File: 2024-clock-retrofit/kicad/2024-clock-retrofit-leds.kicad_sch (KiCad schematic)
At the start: 60 parts, among them Q1 AO3400A, Q2 AO3400A

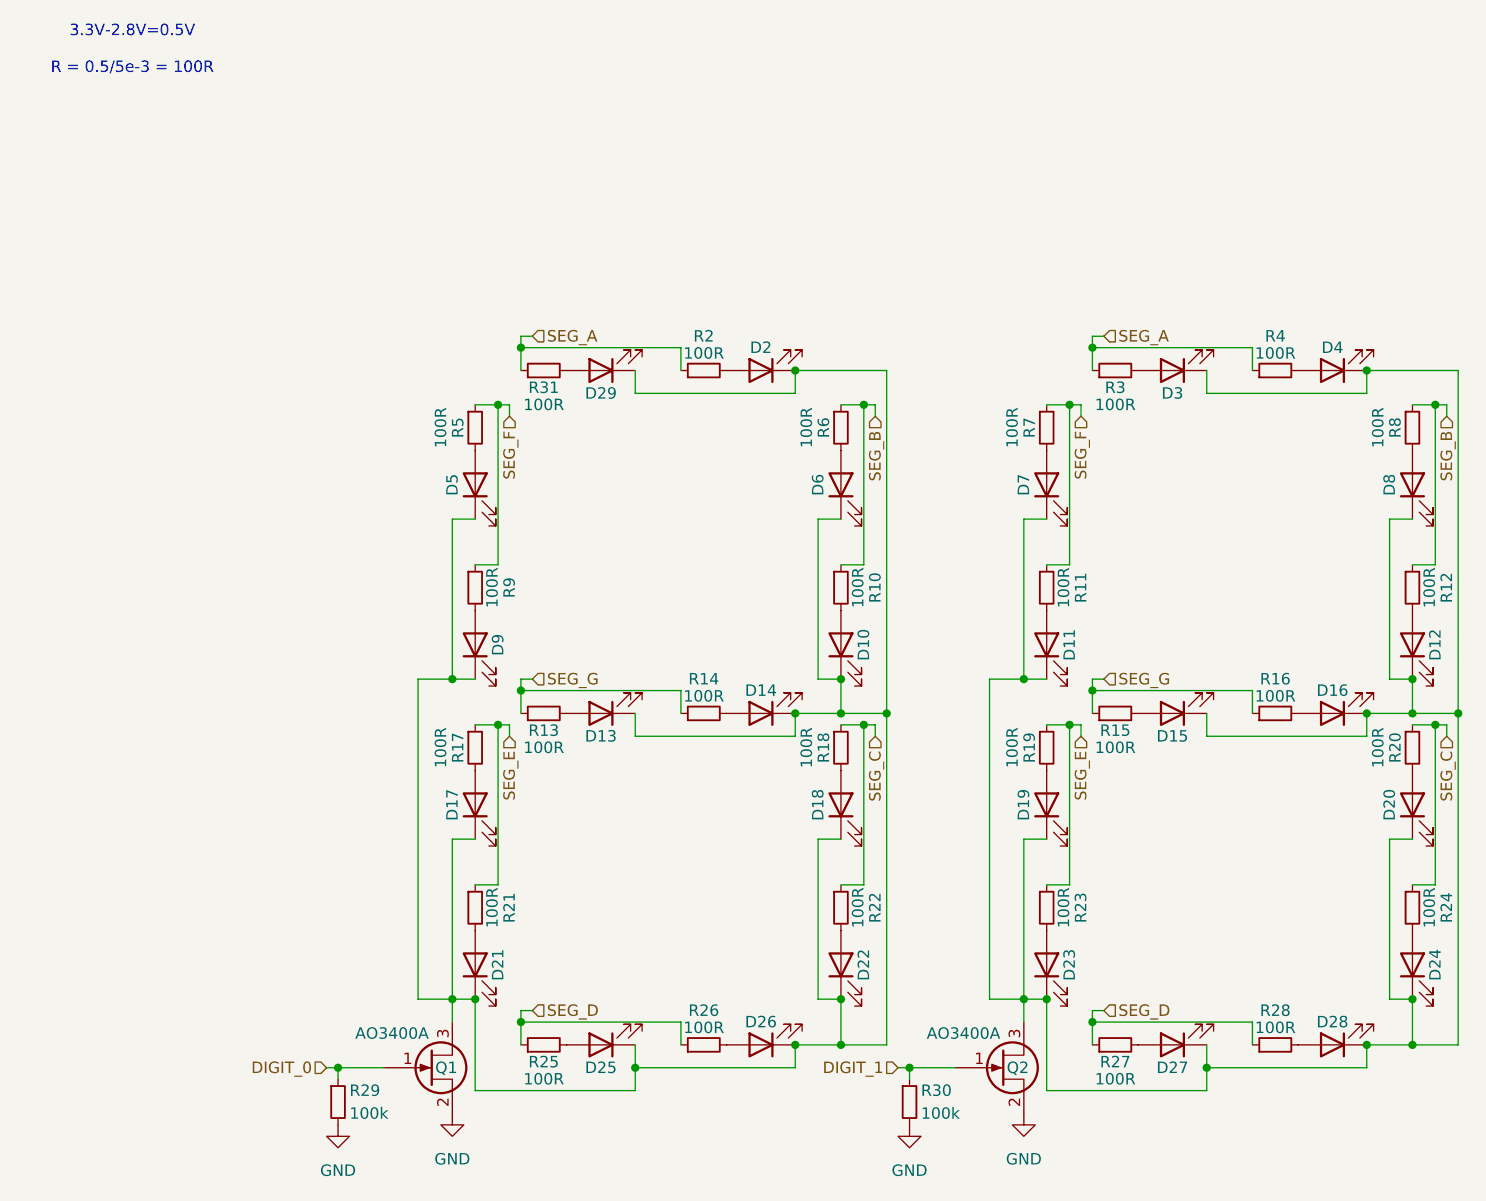
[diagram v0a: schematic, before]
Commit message: 2024-clock-retrofit: ready for jlcpcb
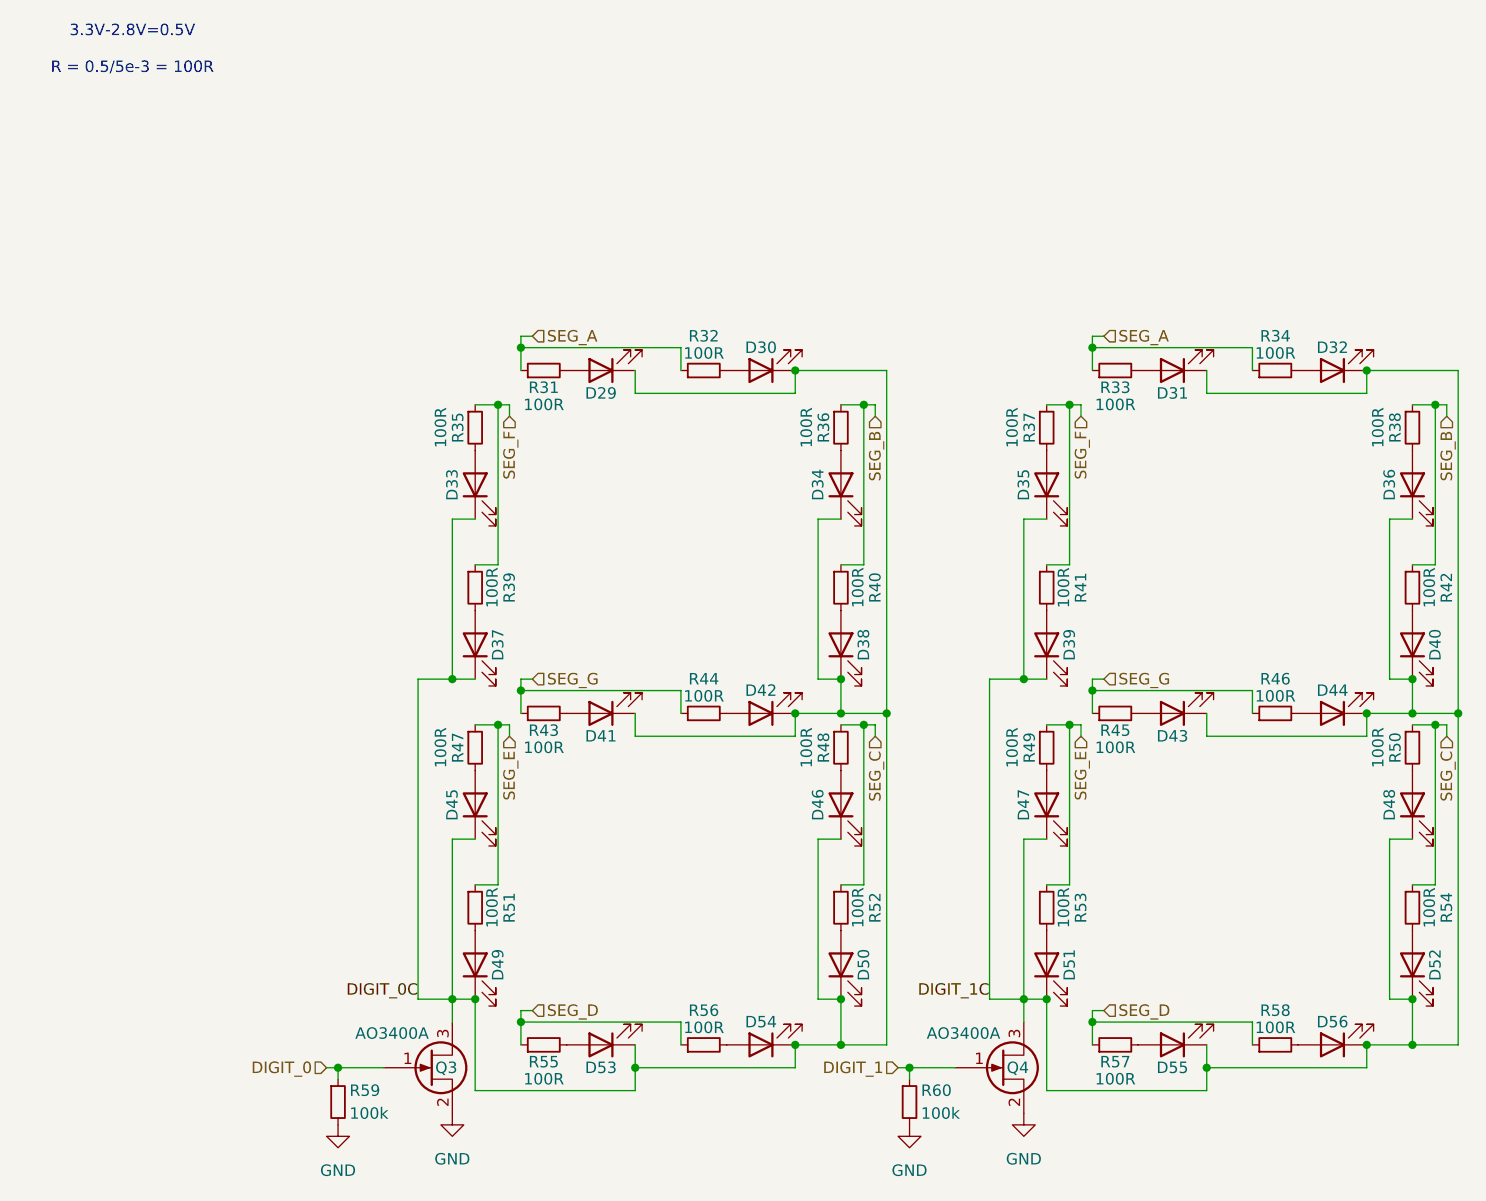
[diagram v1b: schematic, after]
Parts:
- renumbered D2 to D30, D3 to D31, D4 to D32, D5 to D33, D6 to D34, D7 to D35, D8 to D36, D9 to D37, D10 to D38, D11 to D39, D12 to D40, D13 to D41, D14 to D42, D15 to D43, D16 to D44, D17 to D45, D18 to D46, D19 to D47, D20 to D48, D21 to D49, D22 to D50, D23 to D51, D24 to D52, D25 to D53, D26 to D54, D27 to D55, D28 to D56, Q1 to Q3, Q2 to Q4, R2 to R32, R3 to R33, R4 to R34, R5 to R35, R6 to R36, R7 to R37, R8 to R38, R9 to R39, R10 to R40, R11 to R41, R12 to R42, R13 to R43, R14 to R44, R15 to R45, R16 to R46, R17 to R47, R18 to R48, R19 to R49, R20 to R50, R21 to R51, R22 to R52, R23 to R53, R24 to R54, R25 to R55, R26 to R56, R27 to R57, R28 to R58, R29 to R59, R30 to R60
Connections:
- net DIGIT_0C: now reaches D29.1 (K), D30.1 (K), D33.1 (K), D34.1 (K), D37.1 (K), D38.1 (K), D41.1 (K), D42.1 (K), D45.1 (K), D46.1 (K), D49.1 (K), D50.1 (K), D53.1 (K), D54.1 (K), Q3.3 (D)
- net DIGIT_1C: now reaches D31.1 (K), D32.1 (K), D35.1 (K), D36.1 (K), D39.1 (K), D40.1 (K), D43.1 (K), D44.1 (K), D47.1 (K), D48.1 (K), D51.1 (K), D52.1 (K), D55.1 (K), D56.1 (K), Q4.3 (D)
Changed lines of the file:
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@@
 		)
 	)
+	(label "DIGIT_0C"
+		(at 57.15 123.19 180)
+		(fields_autoplaced yes)
+		(effects
+			(font
+				(size 1.27 1.27)
+			)
+			(justify right bottom)
+		)
+	)
+	(label "DIGIT_1C"
+		(at 120.65 123.19 180)
+		(fields_autoplaced yes)
+		(effects
+			(font
+				(size 1.27 1.27)
+			)
+			(justify right bottom)
+		)
+	)
 	(hierarchical_label "SEG_D"
 		(shape input)
@@
 		(on_board yes)
 		(dnp no)
-		(property "Reference" "D17"
+		(property "Reference" "D45"
 			(at 60.96 101.6 0)
 			(effects
@@
 		(on_board yes)
 		(dnp no)
-		(property "Reference" "D10"
+		(property "Reference" "D38"
 			(at 106.68 83.82 0)
 			(effects
@@
 		(on_board yes)
 		(dnp no)
-		(property "Reference" "D24"
+		(property "Reference" "D52"
 			(at 170.18 119.38 0)
 			(effects
@@
 		(on_board yes)
 		(dnp no)
-		(property "Reference" "D14"
+		(property "Reference" "D42"
 			(at 95.25 88.9 0)
 			(effects
@@
 		(on_board yes)
 		(dnp no)
-		(property "Reference" "R16"
+		(property "Reference" "R46"
 			(at 152.4 87.63 90)
 			(effects
@@
 		(on_board yes)
 		(dnp no)
-		(property "Reference" "R25"
+		(property "Reference" "R55"
 			(at 71.12 130.175 90)
 			(effects
@@
 		(dnp no)
 		(fields_autoplaced yes)
-		(property "Reference" "#PWR04"
+		(property "Reference" "#PWR08"
 			(at 111.76 143.51 0)
 			(effects
@@
 		(on_board yes)
 		(dnp no)
-		(property "Reference" "D27"
+		(property "Reference" "D55"
 			(at 140.97 130.81 0)
 			(effects
@@
 		(on_board yes)
 		(dnp no)
-		(property "Reference" "R24"
+		(property "Reference" "R54"
 			(at 171.45 113.03 90)
 			(effects
@@
 		(on_board yes)
 		(dnp no)
-		(property "Reference" "R20"
+		(property "Reference" "R50"
 			(at 165.735 95.25 90)
 			(effects
@@
 		(on_board yes)
 		(dnp no)
-		(property "Reference" "D13"
+		(property "Reference" "D41"
 			(at 77.47 93.98 0)
 			(effects
@@
 		(on_board yes)
 		(dnp no)
-		(property "Reference" "D12"
+		(property "Reference" "D40"
 			(at 170.18 83.82 0)
 			(effects
@@
 		(on_board yes)
 		(dnp no)
-		(property "Reference" "D11"
+		(property "Reference" "D39"
 			(at 129.54 83.82 0)
 			(effects
@@
 		(dnp no)
 		(fields_autoplaced yes)
-		(property "Reference" "#PWR02"
+		(property "Reference" "#PWR06"
 			(at 124.46 142.24 0)
 			(effects
@@
 		(on_board yes)
 		(dnp no)
-		(property "Reference" "D15"
+		(property "Reference" "D43"
 			(at 140.97 93.98 0)
 			(effects
@@
 		(on_board yes)
 		(dnp no)
-		(property "Reference" "R3"
+		(property "Reference" "R33"
 			(at 134.62 55.245 90)
 			(effects
@@
 		(on_board yes)
 		(dnp no)
-		(property "Reference" "R26"
+		(property "Reference" "R56"
 			(at 88.9 124.46 90)
 			(effects
@@
 		(on_board yes)
 		(dnp no)
-		(property "Reference" "D9"
+		(property "Reference" "D37"
 			(at 66.04 83.82 0)
 			(effects
@@
 		(on_board yes)
 		(dnp no)
-		(property "Reference" "Q2"
+		(property "Reference" "Q4"
 			(at 122.555 130.81 0)
 			(effects
@@
 		(on_board yes)
 		(dnp no)
-		(property "Reference" "R27"
+		(property "Reference" "R57"
 			(at 134.62 130.175 90)
 			(effects
@@
 		(on_board yes)
 		(dnp no)
-		(property "Reference" "D4"
+		(property "Reference" "D32"
 			(at 158.75 50.8 0)
 			(effects
@@
 		(dnp no)
 		(fields_autoplaced yes)
-		(property "Reference" "#PWR01"
+		(property "Reference" "#PWR05"
 			(at 60.96 142.24 0)
 			(effects
@@
 		(on_board yes)
 		(dnp no)
-		(property "Reference" "R23"
+		(property "Reference" "R53"
 			(at 130.81 113.03 90)
 			(effects
@@
 		(on_board yes)
 		(dnp no)
-		(property "Reference" "D23"
+		(property "Reference" "D51"
 			(at 129.54 119.38 0)
 			(effects
@@
 		(on_board yes)
 		(dnp no)
-		(property "Reference" "R8"
+		(property "Reference" "R38"
 			(at 165.735 59.69 90)
 			(effects
@@
 		(dnp no)
 		(fields_autoplaced yes)
-		(property "Reference" "#PWR03"
+		(property "Reference" "#PWR07"
 			(at 48.26 143.51 0)
 			(effects
@@
 		(on_board yes)
 		(dnp no)
-		(property "Reference" "R11"
+		(property "Reference" "R41"
 			(at 130.81 77.47 90)
 			(effects
@@
 		(on_board yes)
 		(dnp no)
-		(property "Reference" "D26"
+		(property "Reference" "D54"
 			(at 95.25 125.73 0)
 			(effects
@@
 		(on_board yes)
 		(dnp no)
-		(property "Reference" "R29"
+		(property "Reference" "R59"
 			(at 49.53 133.35 0)
 			(effects
@@
 		(on_board yes)
 		(dnp no)
-		(property "Reference" "R10"
+		(property "Reference" "R40"
 			(at 107.95 77.47 90)
 			(effects
@@
 		(on_board yes)
 		(dnp no)
-		(property "Reference" "D21"
+		(property "Reference" "D49"
 			(at 66.04 119.38 0)
 			(effects
@@
 		(on_board yes)
 		(dnp no)
-		(property "Reference" "R9"
+		(property "Reference" "R39"
 			(at 67.31 77.47 90)
 			(effects
@@
 		(on_board yes)
 		(dnp no)
-		(property "Reference" "R30"
+		(property "Reference" "R60"
 			(at 113.03 133.35 0)
 			(effects
@@
 		(on_board yes)
 		(dnp no)
-		(property "Reference" "R15"
+		(property "Reference" "R45"
 			(at 134.62 93.345 90)
 			(effects
@@
 		(on_board yes)
 		(dnp no)
-		(property "Reference" "R13"
+		(property "Reference" "R43"
 			(at 71.12 93.345 90)
 			(effects
@@
 		(on_board yes)
 		(dnp no)
-		(property "Reference" "D3"
+		(property "Reference" "D31"
 			(at 140.97 55.88 0)
 			(effects
@@
 		(on_board yes)
 		(dnp no)
-		(property "Reference" "R4"
+		(property "Reference" "R34"
 			(at 152.4 49.53 90)
 			(effects
@@
 		(on_board yes)
 		(dnp no)
-		(property "Reference" "D22"
+		(property "Reference" "D50"
 			(at 106.68 119.38 0)
 			(effects
@@
 		(on_board yes)
 		(dnp no)
-		(property "Reference" "Q1"
+		(property "Reference" "Q3"
 			(at 59.055 130.81 0)
 			(effects
@@
 		(on_board yes)
 		(dnp no)
-		(property "Reference" "D6"
+		(property "Reference" "D34"
 			(at 101.6 66.04 0)
 			(effects
@@
 		(on_board yes)
 		(dnp no)
-		(property "Reference" "R6"
+		(property "Reference" "R36"
 			(at 102.235 59.69 90)
 			(effects
@@
 		(on_board yes)
 		(dnp no)
-		(property "Reference" "R21"
+		(property "Reference" "R51"
 			(at 67.31 113.03 90)
 			(effects
@@
 		(on_board yes)
 		(dnp no)
-		(property "Reference" "R28"
+		(property "Reference" "R58"
 			(at 152.4 124.46 90)
 			(effects
@@
 		(on_board yes)
 		(dnp no)
-		(property "Reference" "R2"
+		(property "Reference" "R32"
 			(at 88.9 49.53 90)
 			(effects
@@
 		(on_board yes)
 		(dnp no)
-		(property "Reference" "R22"
+		(property "Reference" "R52"
 			(at 107.95 113.03 90)
 			(effects
@@
 		(on_board yes)
 		(dnp no)
-		(property "Reference" "D16"
+		(property "Reference" "D44"
 			(at 158.75 88.9 0)
 			(effects
@@
 		(on_board yes)
 		(dnp no)
-		(property "Reference" "R17"
+		(property "Reference" "R47"
 			(at 61.595 95.25 90)
 			(effects
@@
 		(on_board yes)
 		(dnp no)
-		(property "Reference" "R5"
+		(property "Reference" "R35"
 			(at 61.595 59.69 90)
 			(effects
@@
 		(on_board yes)
 		(dnp no)
-		(property "Reference" "R18"
+		(property "Reference" "R48"
 			(at 102.235 95.25 90)
 			(effects
@@
 		(on_board yes)
 		(dnp no)
-		(property "Reference" "D18"
+		(property "Reference" "D46"
 			(at 101.6 101.6 0)
 			(effects
@@
 		(on_board yes)
 		(dnp no)
-		(property "Reference" "D8"
+		(property "Reference" "D36"
 			(at 165.1 66.04 0)
 			(effects
@@
 		(on_board yes)
 		(dnp no)
-		(property "Reference" "R14"
+		(property "Reference" "R44"
 			(at 88.9 87.63 90)
 			(effects
@@
 		(on_board yes)
 		(dnp no)
-		(property "Reference" "D28"
+		(property "Reference" "D56"
 			(at 158.75 125.73 0)
 			(effects
@@
 		(on_board yes)
 		(dnp no)
-		(property "Reference" "D25"
+		(property "Reference" "D53"
 			(at 77.47 130.81 0)
 			(effects
@@
 		(on_board yes)
 		(dnp no)
-		(property "Reference" "R19"
+		(property "Reference" "R49"
 			(at 125.095 95.25 90)
 			(effects
@@
 		(on_board yes)
 		(dnp no)
-		(property "Reference" "D5"
+		(property "Reference" "D33"
 			(at 60.96 66.04 0)
 			(effects
@@
 		(on_board yes)
 		(dnp no)
-		(property "Reference" "D7"
+		(property "Reference" "D35"
 			(at 124.46 66.04 0)
 			(effects
@@
 		(on_board yes)
 		(dnp no)
-		(property "Reference" "D20"
+		(property "Reference" "D48"
 			(at 165.1 101.6 0)
 			(effects
@@
 		(on_board yes)
 		(dnp no)
-		(property "Reference" "R7"
+		(property "Reference" "R37"
 			(at 125.095 59.69 90)
 			(effects
@@
 		(on_board yes)
 		(dnp no)
-		(property "Reference" "D2"
+		(property "Reference" "D30"
 			(at 95.25 50.8 0)
 			(effects
@@
 		(on_board yes)
 		(dnp no)
-		(property "Reference" "D19"
+		(property "Reference" "D47"
 			(at 124.46 101.6 0)
 			(effects
@@
 		(on_board yes)
 		(dnp no)
-		(property "Reference" "R12"
+		(property "Reference" "R42"
 			(at 171.45 77.47 90)
 			(effects

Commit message: 2024-clock-retrofit: as submitted April 2025
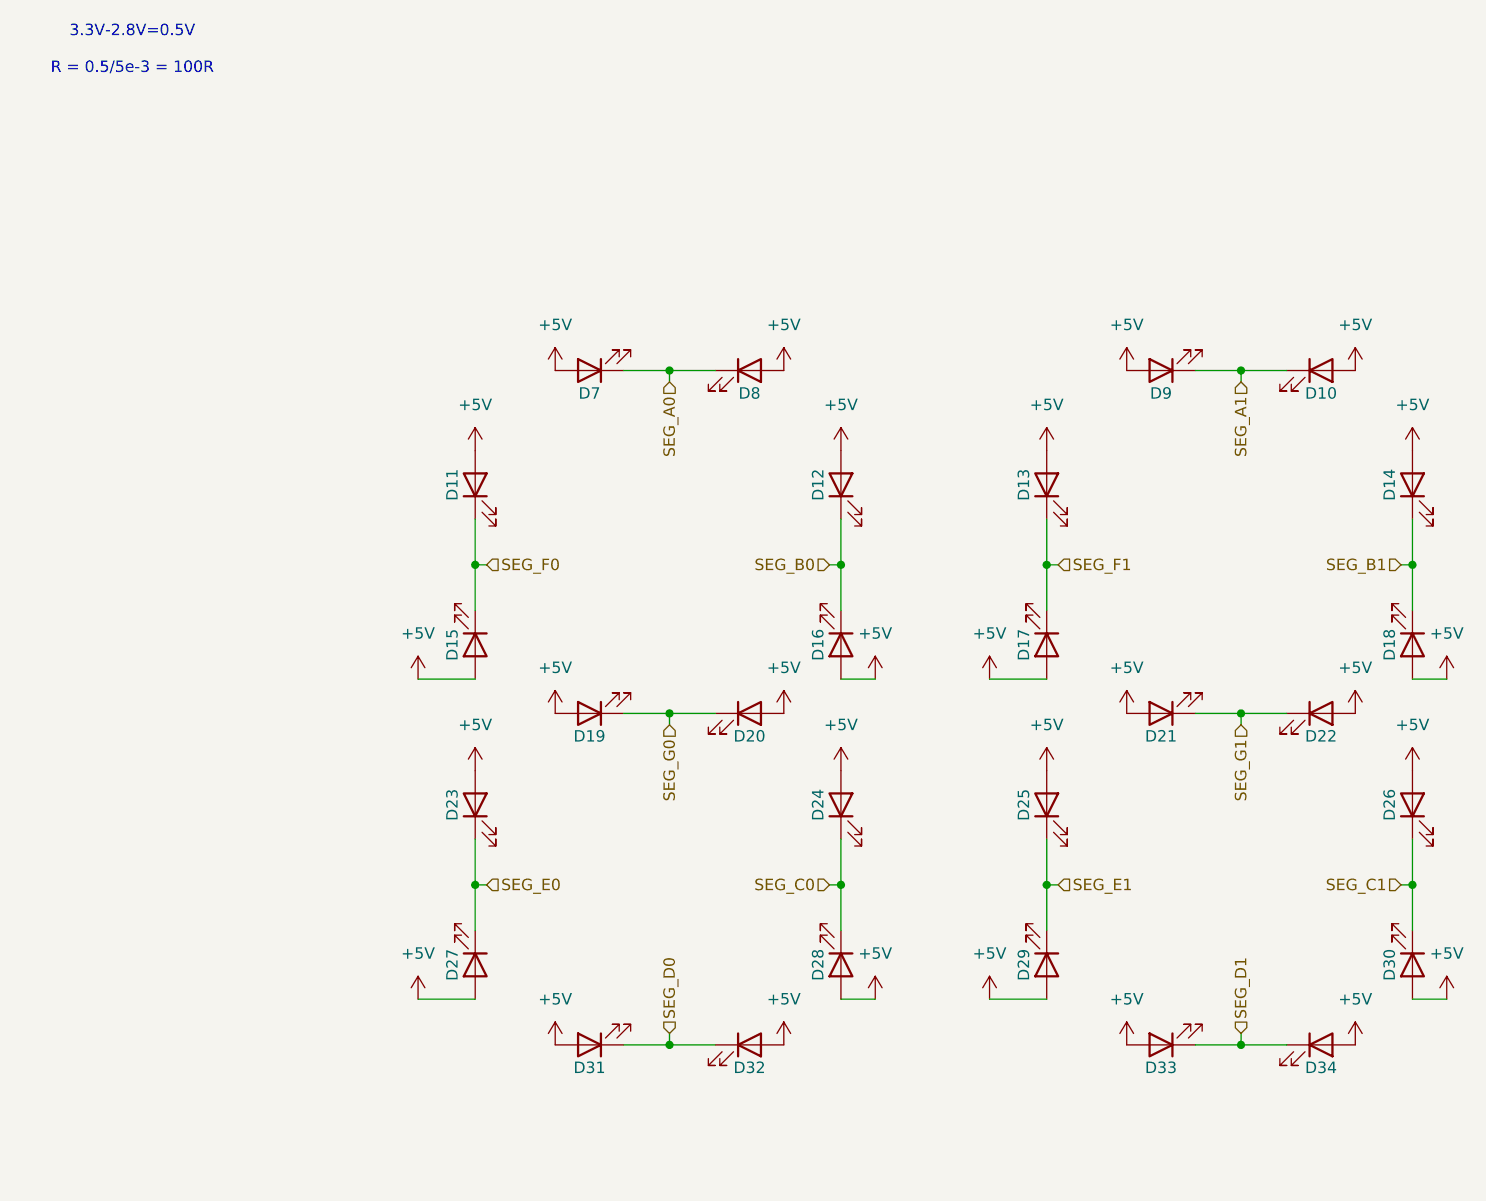
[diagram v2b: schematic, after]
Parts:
- removed Q3, Q4: AO3400A, library:SOT-23, symbol library:AO3400A
- removed R31, R32, R33, R34, R35, R36, R37, R38, R39, R40, R41, R42, R43, R44, R45, R46, R47, R48, R49, R50, R51, R52, R53, R54, R55, R56, R57, R58: 100R, library:R_0402_1005Metric, symbol library:R_100R
- removed R59, R60: 100k, library:R_0402_1005Metric, symbol library:R_100k
- renumbered D32 to D10, D33 to D11, D34 to D12, D35 to D13, D36 to D14, D37 to D15, D38 to D16, D39 to D17, D40 to D18, D41 to D19, D42 to D20, D43 to D21, D44 to D22, D45 to D23, D46 to D24, D47 to D25, D48 to D26, D49 to D27, D50 to D28, D51 to D29, D52 to D30, D53 to D31, D54 to D32, D55 to D33, D56 to D34, D29 to D7, D30 to D8, D31 to D9
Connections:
- net +5V: now reaches D23.2 (A)
- net +5V: now also D10.2 (A), D11.2 (A), D12.2 (A), D13.2 (A), D14.2 (A), D15.2 (A), D16.2 (A), D17.2 (A), D18.2 (A), D19.2 (A), D20.2 (A), D21.2 (A), D22.2 (A), D24.2 (A), D25.2 (A), D26.2 (A), D27.2 (A), D28.2 (A), D29.2 (A), D30.2 (A), D31.2 (A), D32.2 (A), D33.2 (A), D34.2 (A), D7.2 (A), D8.2 (A), D9.2 (A)
- removed net DIGIT_0C: D11.1 (K), D12.1 (K), D15.1 (K), D16.1 (K), D19.1 (K), D20.1 (K), D23.1 (K), D24.1 (K), D27.1 (K), D28.1 (K), D31.1 (K), D32.1 (K), D7.1 (K), D8.1 (K)
- removed net DIGIT_1C: D10.1 (K), D13.1 (K), D14.1 (K), D17.1 (K), D18.1 (K), D21.1 (K), D22.1 (K), D25.1 (K), D26.1 (K), D29.1 (K), D30.1 (K), D33.1 (K), D34.1 (K), D9.1 (K)
- new net SEG_A0: D7.1 (K), D8.1 (K)
- new net SEG_A1: D10.1 (K), D9.1 (K)
- new net SEG_B0: D12.1 (K), D16.1 (K)
- new net SEG_B1: D14.1 (K), D18.1 (K)
- new net SEG_C0: D24.1 (K), D28.1 (K)
- new net SEG_C1: D26.1 (K), D30.1 (K)
- new net SEG_D0: D31.1 (K), D32.1 (K)
- new net SEG_D1: D33.1 (K), D34.1 (K)
- new net SEG_E0: D23.1 (K), D27.1 (K)
- new net SEG_E1: D25.1 (K), D29.1 (K)
- new net SEG_F0: D11.1 (K), D15.1 (K)
- new net SEG_F1: D13.1 (K), D17.1 (K)
- new net SEG_G0: D19.1 (K), D20.1 (K)
- new net SEG_G1: D21.1 (K), D22.1 (K)
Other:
- moved on the sheet: D10, D15, D16, D17, D18, D19, D20, D21, D22, D27, D28, D29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
